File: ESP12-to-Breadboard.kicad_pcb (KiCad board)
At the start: 2 copper layers, 22.9 x 20.1 mm, 3 parts, among them J1 Conn_01x08, J2 Conn_01x08

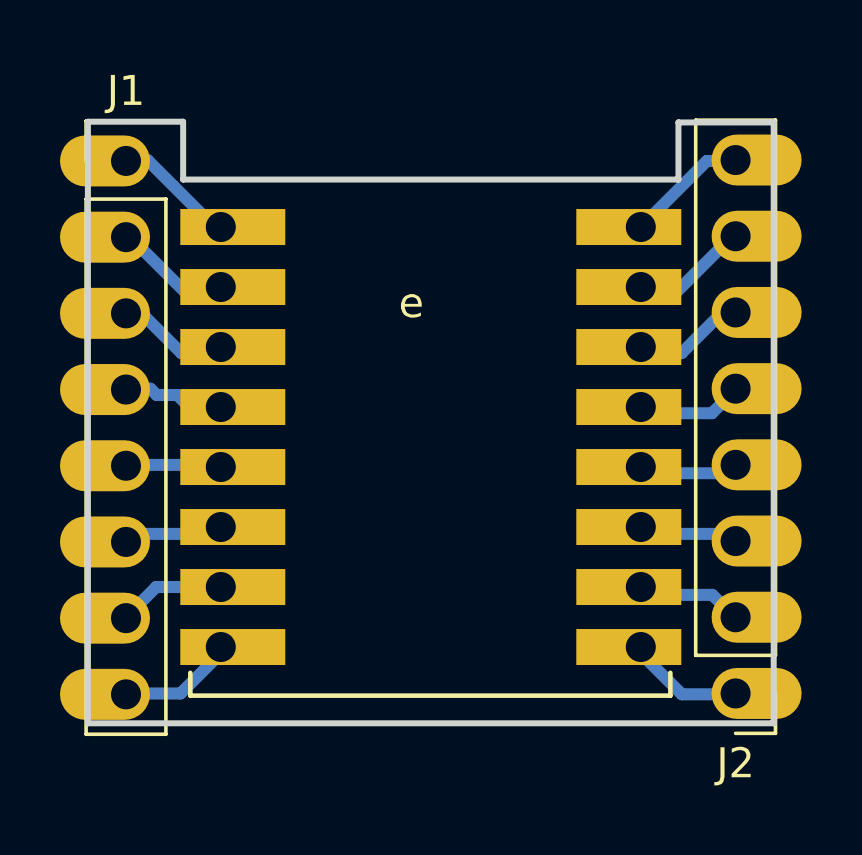
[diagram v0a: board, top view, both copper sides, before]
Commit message: Fix orientation of the headers
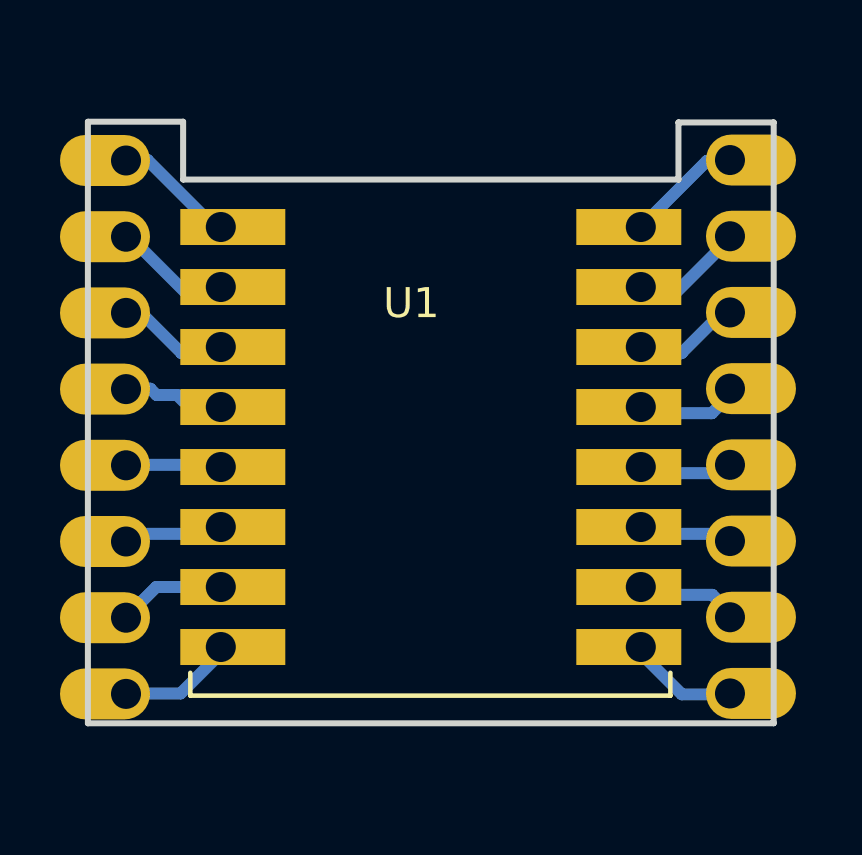
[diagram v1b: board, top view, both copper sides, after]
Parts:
- J1: renamed from J2; moved to B.Cu
- J2: renamed from J1; moved to B.Cu
- moved J1 27.0 mm to (135.9, 74.9)
- moved J2 26.8 mm to (156.0, 92.7)
- renumbered e to U1
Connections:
- J1 pad 1: Net-(U1-Pad9) -> Net-(J1-Pad1)
- J1 pad 2: Net-(U1-Pad10) -> Net-(J1-Pad2)
- J1 pad 3: Net-(U1-Pad11) -> Net-(J1-Pad3)
- J1 pad 4: Net-(U1-Pad12) -> Net-(J1-Pad4)
- J1 pad 5: Net-(U1-Pad13) -> Net-(J1-Pad5)
- J1 pad 6: Net-(U1-Pad14) -> Net-(J1-Pad6)
- J1 pad 7: Net-(U1-Pad15) -> Net-(J1-Pad7)
- J1 pad 8: Net-(U1-Pad16) -> Net-(J1-Pad8)
- J2 pad 1: Net-(J1-Pad1) -> Net-(J2-Pad1)
- J2 pad 2: Net-(J1-Pad2) -> Net-(J2-Pad2)
- J2 pad 3: Net-(J1-Pad3) -> Net-(J2-Pad3)
- J2 pad 4: Net-(J1-Pad4) -> Net-(J2-Pad4)
- J2 pad 5: Net-(J1-Pad5) -> Net-(J2-Pad5)
- J2 pad 6: Net-(J1-Pad6) -> Net-(J2-Pad6)
- J2 pad 7: Net-(J1-Pad7) -> Net-(J2-Pad7)
- J2 pad 8: Net-(J1-Pad8) -> Net-(J2-Pad8)
- U1 pad 10: Net-(U1-Pad10) -> Net-(J2-Pad2)
- U1 pad 11: Net-(U1-Pad11) -> Net-(J2-Pad3)
- U1 pad 12: Net-(U1-Pad12) -> Net-(J2-Pad4)
- U1 pad 13: Net-(U1-Pad13) -> Net-(J2-Pad5)
- U1 pad 14: Net-(U1-Pad14) -> Net-(J2-Pad6)
- U1 pad 15: Net-(U1-Pad15) -> Net-(J2-Pad7)
- U1 pad 16: Net-(U1-Pad16) -> Net-(J2-Pad8)
- U1 pad 9: Net-(U1-Pad9) -> Net-(J2-Pad1)
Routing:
- net Net-(U1-Pad16): track 4.28 -> 0.00 mm
- net Net-(J2-Pad8): track 0.00 -> 4.28 mm
- net Net-(U1-Pad15): track 3.93 -> 0.00 mm
- net Net-(J2-Pad7): track 0.00 -> 3.93 mm
- net Net-(U1-Pad9): track 3.73 -> 0.00 mm
- net Net-(J2-Pad1): track 0.00 -> 3.73 mm
- net Net-(U1-Pad14): track 3.71 -> 0.00 mm
- net Net-(J2-Pad6): track 0.00 -> 3.71 mm
- net Net-(U1-Pad10): track 3.50 -> 0.00 mm
- net Net-(J2-Pad2): track 0.00 -> 3.50 mm
- net Net-(U1-Pad13): track 3.49 -> 0.00 mm
- net Net-(J2-Pad5): track 0.00 -> 3.49 mm
- net Net-(U1-Pad11): track 3.28 -> 0.00 mm
- net Net-(J2-Pad3): track 0.00 -> 3.28 mm
- net Net-(U1-Pad12): track 3.26 -> 0.00 mm
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
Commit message: Prepare for plotting
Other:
- board size 22.9 x 20.1 mm -> 22.9 x 20.4 mm
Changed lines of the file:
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@@
     (pad_to_mask_clearance 0)
     (pcbplotparams
-      (layerselection 0x00010fc_ffffffff)
+      (layerselection 0x0000000_fffffffe)
       (disableapertmacros false)
       (usegerberextensions false)
@@
       (hpglpendiameter 15.000000)
       (dxfpolygonmode true)
-      (dxfimperialunits true)
+      (dxfimperialunits false)
       (dxfusepcbnewfont true)
       (psnegative false)
@@
       (sketchpadsonfab false)
       (subtractmaskfromsilk false)
-      (outputformat 1)
+      (outputformat 3)
       (mirror false)
-      (drillshape 1)
+      (drillshape 0)
       (scaleselection 1)
-      (outputdirectory "")
+      (outputdirectory "plot")
     )
   )
@@
     (property "Sheetname" "")
     (attr through_hole)
-    (fp_text reference "U1" (at 6.35 2.54) (layer "F.SilkS")
+    (fp_text reference "U1" (at 6.95 -0.147) (layer "F.SilkS")
       (effects (font (size 1 1) (thickness 0.15)))
     )
@@
     (fp_line (start 1.27 -19.05) (end -1.27 -19.05) (layer "B.Fab") (width 0.1))
     (fp_line (start -1.27 0.635) (end -0.635 1.27) (layer "B.Fab") (width 0.1))
-    (pad "1" thru_hole oval (at 0 0) (size 3 1.7) (drill 1 (offset 0.7 0)) (layers *.Cu *.Mask)
+    (pad "1" thru_hole oval (at 0 0) (size 3 1.7) (drill 0.8 (offset 0.7 0)) (layers *.Cu *.Mask)
       (net 16 "Net-(J2-Pad1)") (pinfunction "Pin_1") (pintype "passive"))
     (pad "2" thru_hole oval (at 0 -2.54) (size 3 1.7) (drill 1 (offset 0.7 0)) (layers *.Cu *.Mask)
@@
   (gr_poly
     (pts
+      (xy 137.794998 75.565)
+      (xy 154.304998 75.565)
+      (xy 154.304998 73.66)
+      (xy 157.479998 73.66)
+      (xy 157.479998 93.689919)
+      (xy 153 93.689919)
+      (xy 153 92)
+      (xy 151 92)
+      (xy 151 90)
+      (xy 141 90)
+      (xy 141 92)
+      (xy 139 92)
+      (xy 139 94)
+      (xy 134.619999 94)
+      (xy 134.619999 73.63693)
+      (xy 137.794998 73.63693)
+    ) (layer "Edge.Cuts") (width 0.1) (fill none))
+  (gr_poly
+    (pts
